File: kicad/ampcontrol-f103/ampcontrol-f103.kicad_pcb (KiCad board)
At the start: 2 copper layers, 89.3 x 55 mm, 69 parts, among them J1 SP, J10 Buttons, J11 Encoder, J12 LCD_CTRL, J13 I2C, J14 I2C, J15 I2C, J16 SPI_2.4, J17 SPI_2.8, J18 SPI_3.2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

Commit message: Kicad PCB: Fix missing connection for sdcard socket
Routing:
- net /SD_SCK: track 109.1 -> 115.7 mm
- net /SD_MOSI: track 124.4 -> 127.7 mm
- net /SD_MISO: track 118.9 -> 122.2 mm
- net /SD_CS: track 126.0 -> 129.3 mm
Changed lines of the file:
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@@
     (thickness 1.6)
     (drawings 35)
-    (tracks 1268)
+    (tracks 1273)
     (zones 0)
     (modules 69)
@@
   )
   (setup
-    (last_trace_width 0.25)
+    (last_trace_width 0.6)
     (user_trace_width 0.4)
     (user_trace_width 0.6)
@@
   (segment (start 172.239988 102.809988) (end 143.203012 102.809988) (width 0.4) (layer F.Cu) (net 30))
   (segment (start 169.92 77.32) (end 171.85 77.32) (width 0.4) (layer F.Cu) (net 30))
+  (segment (start 177.74 77.32) (end 181.04 77.32) (width 0.6) (layer F.Cu) (net 30))
   (segment (start 125.17 64.31) (end 122.63 66.85) (width 0.4) (layer B.Cu) (net 31) (status 20))
   (segment (start 125.17 63.04) (end 125.17 64.31) (width 0.4) (layer B.Cu) (net 31) (status 10))
@@
   (segment (start 173.340011 84.259989) (end 173.340011 102.558531) (width 0.4) (layer F.Cu) (net 56))
   (segment (start 177.74 79.86) (end 173.340011 84.259989) (width 0.4) (layer F.Cu) (net 56))
+  (segment (start 177.74 79.86) (end 181.04 79.86) (width 0.6) (layer F.Cu) (net 56))
   (segment (start 129.595 77.105) (end 129.595 75.4388) (width 0.25) (layer F.Cu) (net 57) (status 10))
   (segment (start 129.595 74.636741) (end 132.15173 72.080011) (width 0.25) (layer F.Cu) (net 57))
@@
   (segment (start 174.339988 102.461469) (end 172.752458 104.048999) (width 0.4) (layer F.Cu) (net 57))
   (segment (start 177.74 82.4) (end 176.537919 82.4) (width 0.4) (layer F.Cu) (net 57))
+  (segment (start 177.74 82.4) (end 181.04 82.4) (width 0.6) (layer F.Cu) (net 57))
   (segment (start 130.095 75.9645) (end 130.095 77.105) (width 0.25) (layer F.Cu) (net 58) (status 20))
   (segment (start 130.095 77.105) (end 130.095 75.875) (width 0.25) (layer F.Cu) (net 58) (status 10))
@@
   (segment (start 175.71 84.94) (end 174.939999 85.710001) (width 0.4) (layer F.Cu) (net 58))
   (segment (start 177.74 84.94) (end 175.71 84.94) (width 0.4) (layer F.Cu) (net 58))
+  (segment (start 177.74 84.94) (end 181.04 84.94) (width 0.6) (layer F.Cu) (net 58))
+  (segment (start 177.74 84.94) (end 181.04 84.94) (width 0.6) (layer B.Cu) (net 58))
   (segment (start 168.65 90.02) (end 166.4125 90.02) (width 0.25) (layer B.Cu) (net 59) (status 30))
   (segment (start 168.65 92.56) (end 166.4125 92.56) (width 0.25) (layer B.Cu) (net 60) (status 30))

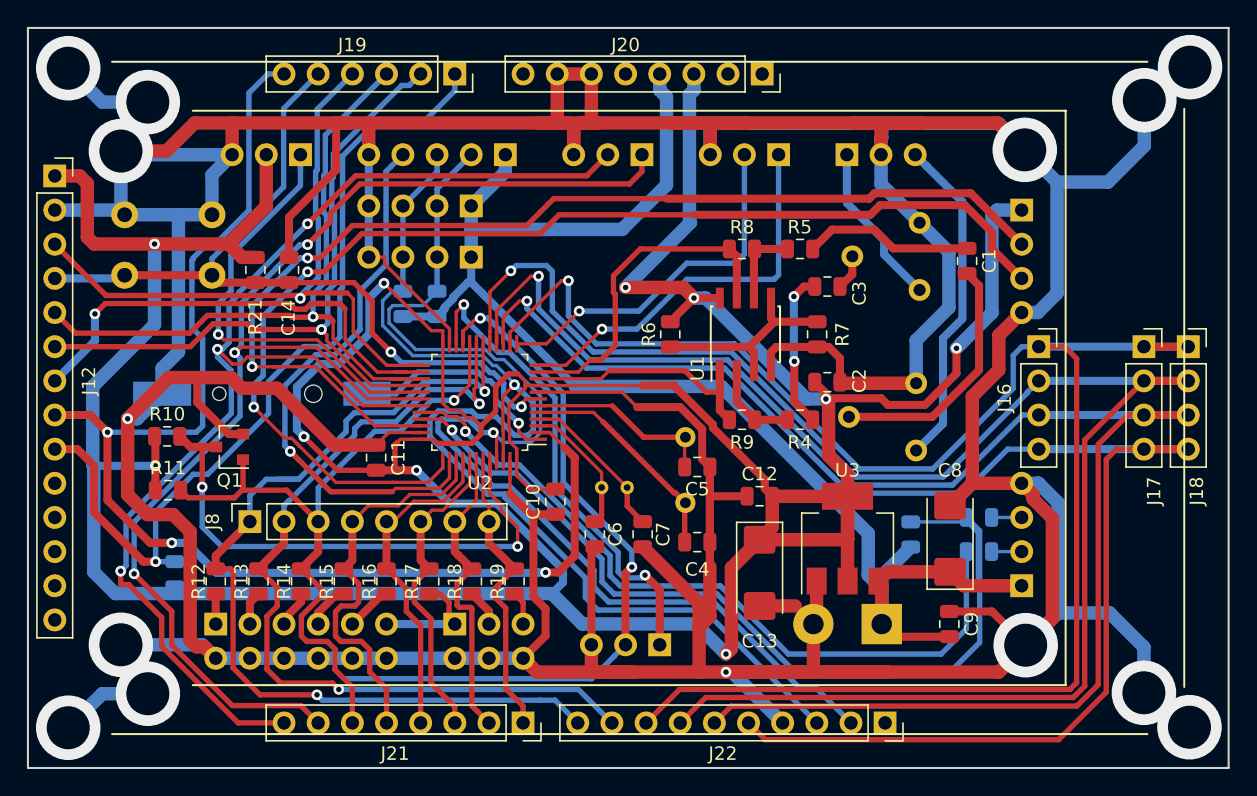
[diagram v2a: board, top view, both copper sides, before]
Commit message: Kicad: Fix arduino-specific pinout
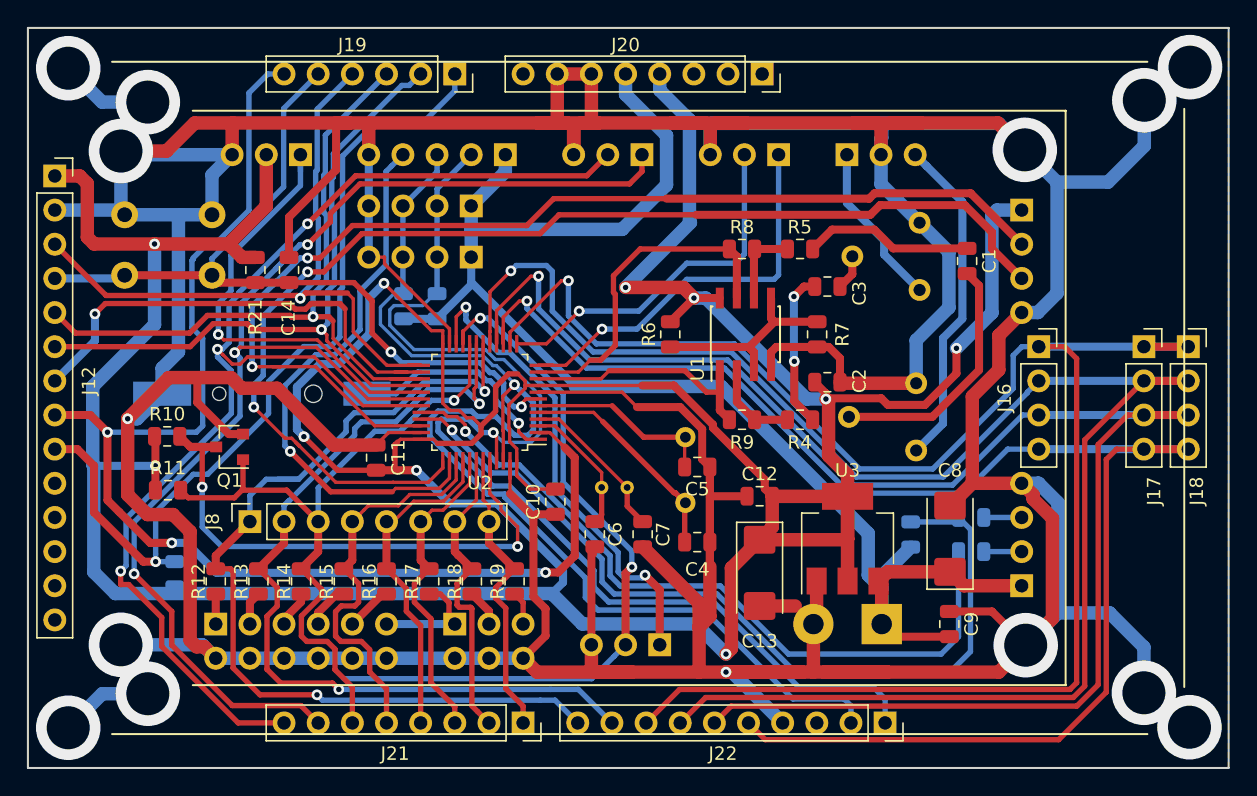
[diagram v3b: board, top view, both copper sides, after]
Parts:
- moved R1 0.58 mm to (164.9, 92.6)
- moved R2 0.58 mm to (164.9, 90.0)
- moved R22 0.18 mm to (122.7, 74.3)
- moved R23 0.17 mm to (125.2, 74.3)
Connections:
- J20 pad 3: +3V3 -> Net-(J20-Pad3)
- J20 pad 4: +5V -> +3V3
- J20 pad 5: Net-(J20-Pad5) -> +5V
- J22 pad 1: Net-(J22-Pad1) -> /SCL
- J22 pad 2: /SCL -> /SDA
- J22 pad 3: /SDA -> Net-(J22-Pad3)
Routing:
- net /USB_DP: track 70.4 -> 64.3 mm
- net /SCL: track 84.6 -> 88.4 mm
- net /SDA: track 85.3 -> 88.6 mm
- net +5V: track 116.5 -> 117.6 mm
- net +3V3: track 345.1 -> 345.8 mm
- net /USB_P: track 2.24 -> 2.82 mm
- net /USB_M: track 2.24 -> 2.82 mm

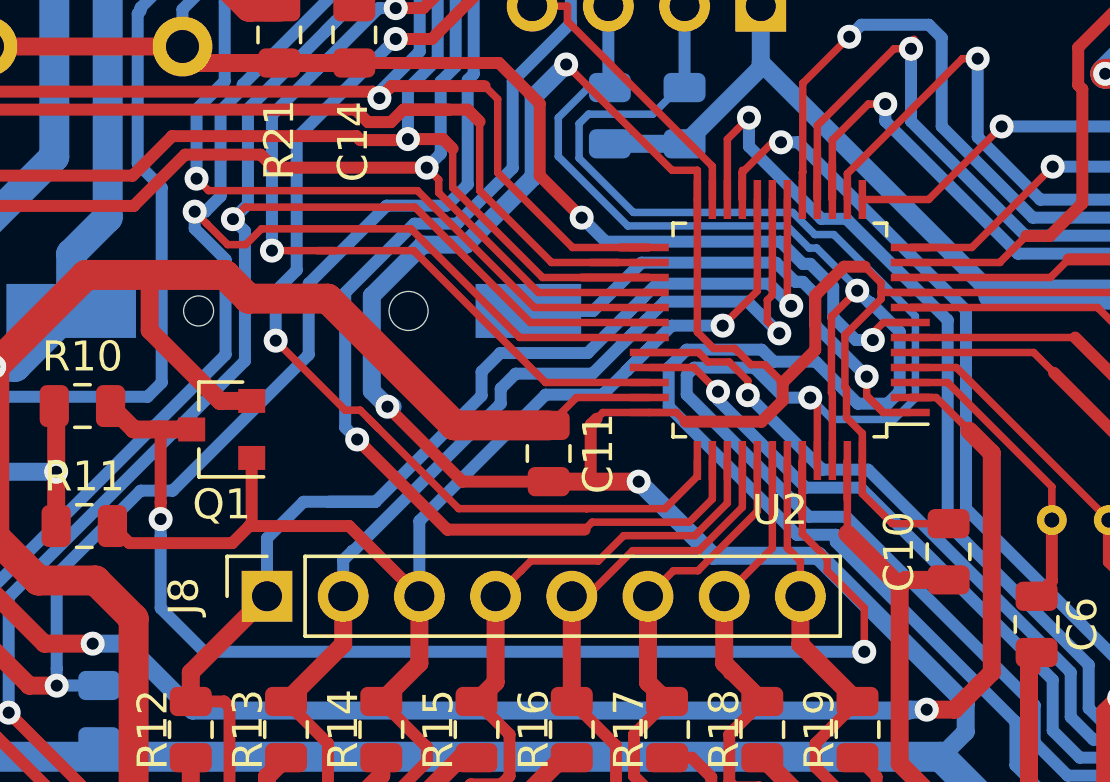
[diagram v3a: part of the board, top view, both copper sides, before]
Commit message: Smal fix for CR1220 package
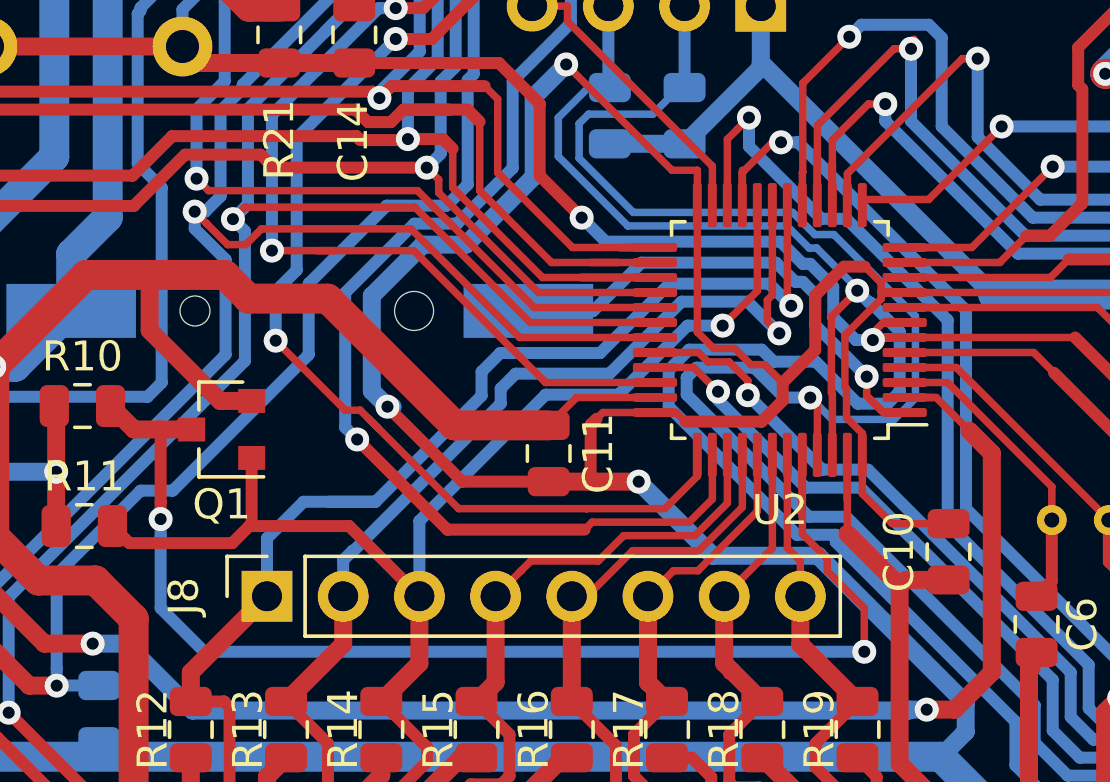
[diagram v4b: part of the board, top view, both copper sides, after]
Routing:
- net /DB1: track 65.8 -> 64.7 mm
- net /DB2: track 54.7 -> 53.6 mm
- net /DB0: track 71.2 -> 70.4 mm

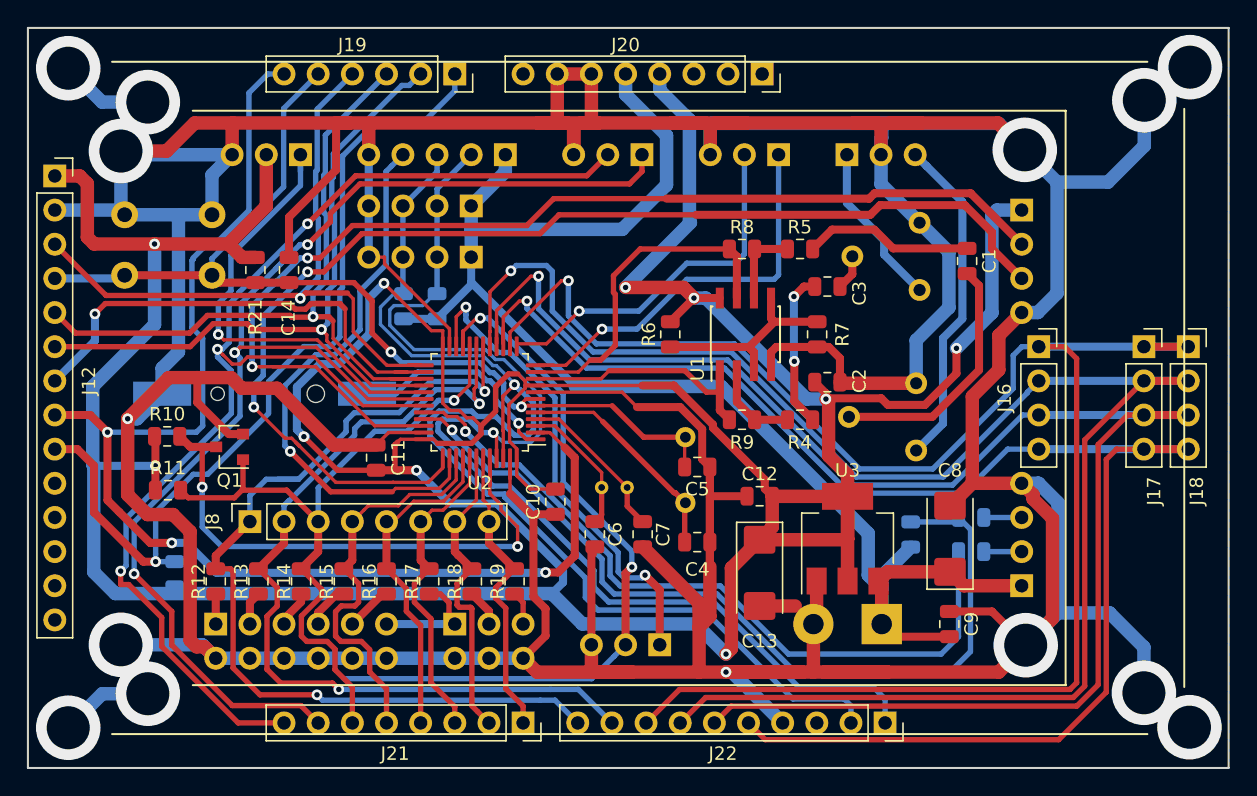
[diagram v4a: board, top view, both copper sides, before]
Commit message: Fix PCB bugs
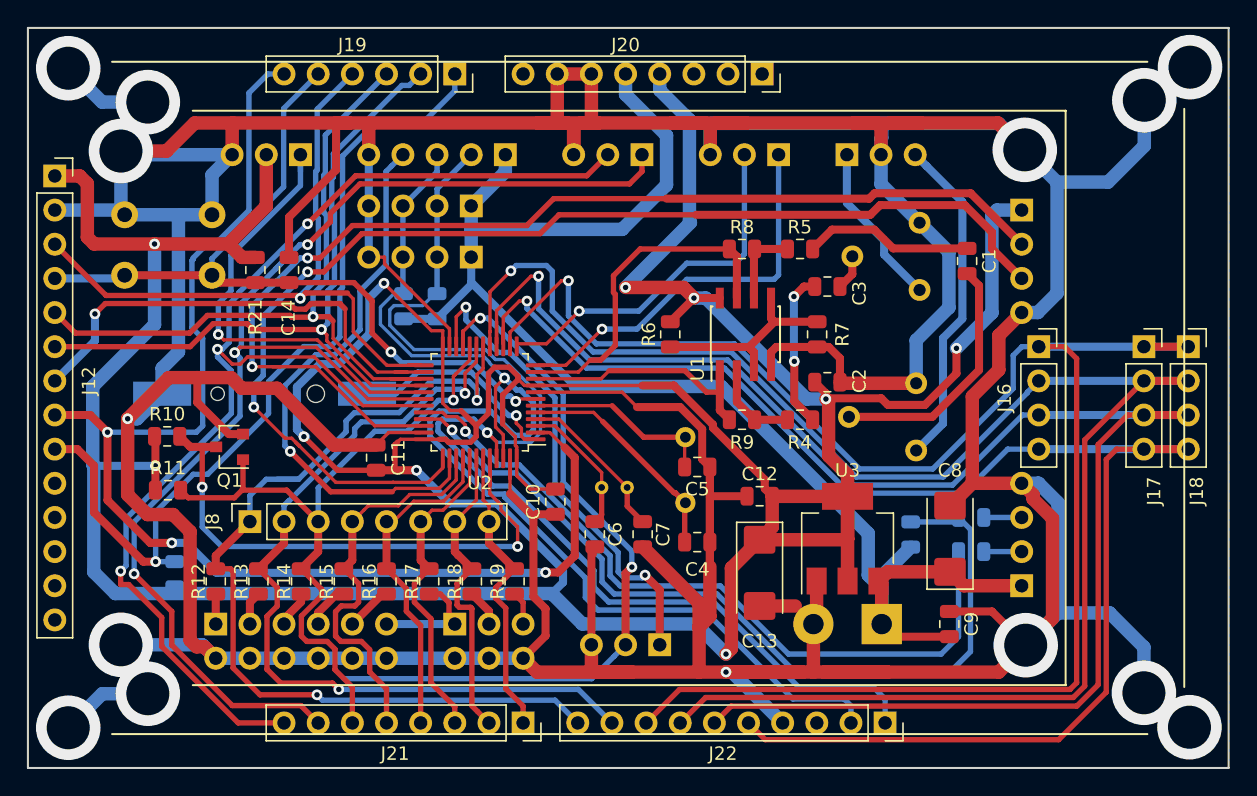
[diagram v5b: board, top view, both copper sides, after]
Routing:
- net /DB1: track 64.7 -> 62.7 mm
- net +3V3: track 345.8 -> 347.3 mm
- net /NRST: track 60.7 -> 59.5 mm
- net /DB0: track 70.4 -> 71.4 mm
- net /SCL: track 88.4 -> 89.2 mm

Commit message: Schematic: map MUTE/STBY to PB11/PB10, that are de-facto have been used
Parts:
- J2: value MUTE_STBY -> SWD
- J6: value UART3 -> STBY_MUTE
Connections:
- J2 pad 2: /MUTE -> /SWDIO
- J2 pad 3: /STBY -> /SWCLK
- J6 pad 1: /TX3 -> /STBY
- J6 pad 2: /RX3 -> /MUTE
- U2 pad 21: /RX3 -> /MUTE
- U2 pad 22: /TX3 -> /STBY
- U2 pad 34: /MUTE -> /SWDIO
- U2 pad 37: /STBY -> /SWCLK
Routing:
- net /SWCLK: track 0.00 -> 87.6 mm, vias 0 -> 2
- net /SWDIO: track 0.00 -> 82.3 mm, vias 0 -> 2
- net /RX3: track 55.5 -> 0.00 mm, vias 2 -> 0
- net /STBY: track 87.6 -> 35.8 mm
- net /TX3: track 35.8 -> 0.00 mm, vias 2 -> 0
- net /MUTE: track 82.3 -> 55.5 mm

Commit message: Small changes in schematic/PCB
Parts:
- added R24: 0, Resistor_SMD:R_0805_2012Metric, F.Cu at (102.4, 74.8)
- added R25: 0, Resistor_SMD:R_0805_2012Metric, F.Cu at (102.4, 77.4)
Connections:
- J12 pad 4: /NRST -> /RST
- J19 pad 5: /NRST -> /RST
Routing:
- net /RST: track 0.00 -> 36.7 mm, vias 0 -> 2
- net /NRST: track 59.5 -> 39.1 mm
- net /HW_RST: track 41.5 -> 59.6 mm, vias 1 -> 2
- net GNDD: track 622.8 -> 615.3 mm
- net /RS: track 55.4 -> 62.2 mm
- net /WR: track 52.7 -> 58.0 mm
- net /SCK: track 37.0 -> 32.6 mm
- net +3V3: track 347.3 -> 350.4 mm
- net /CS: track 53.2 -> 55.3 mm
- net /RX1: track 93.1 -> 91.3 mm
- net /TX1: track 95.1 -> 94.2 mm
- net /BCKL: track 96.2 -> 95.5 mm
- net /RD: track 63.8 -> 64.4 mm
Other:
- board text added: "+ -"

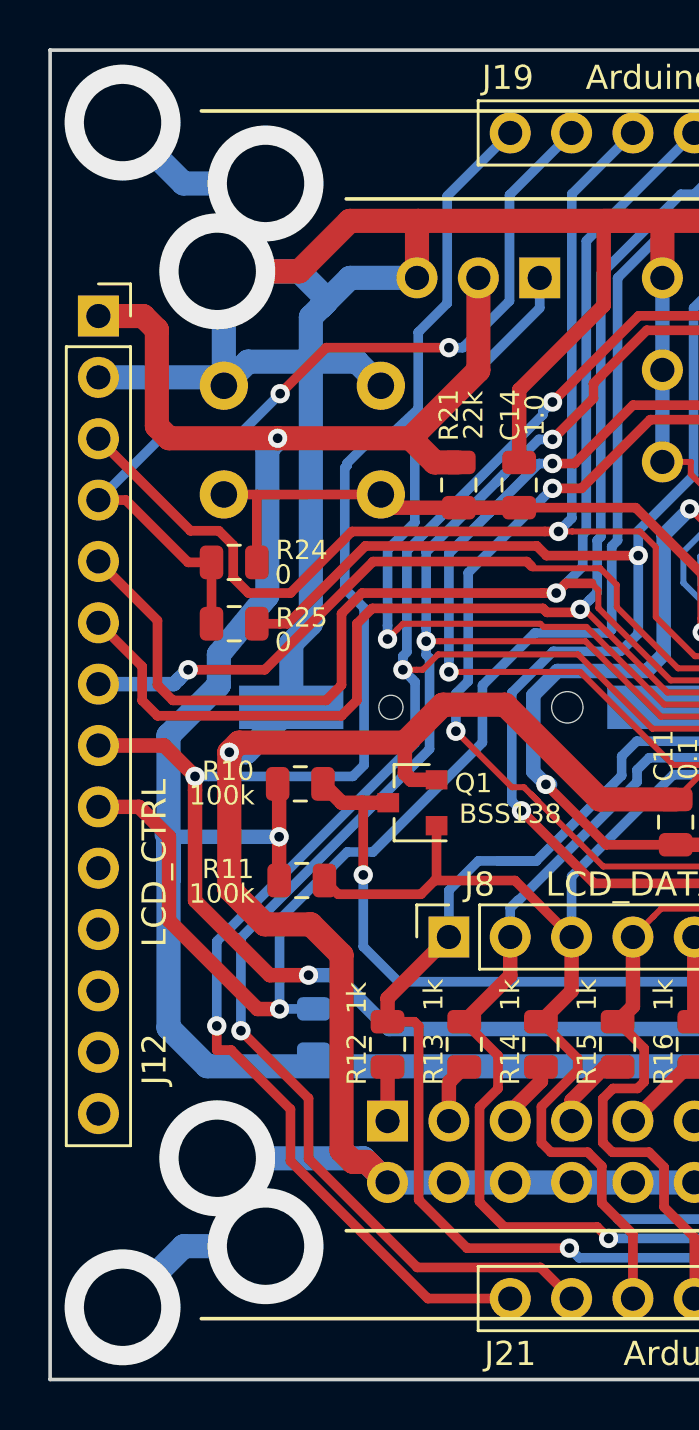
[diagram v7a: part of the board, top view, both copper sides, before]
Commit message: Fix mounting holes on PCB for 2.8 display
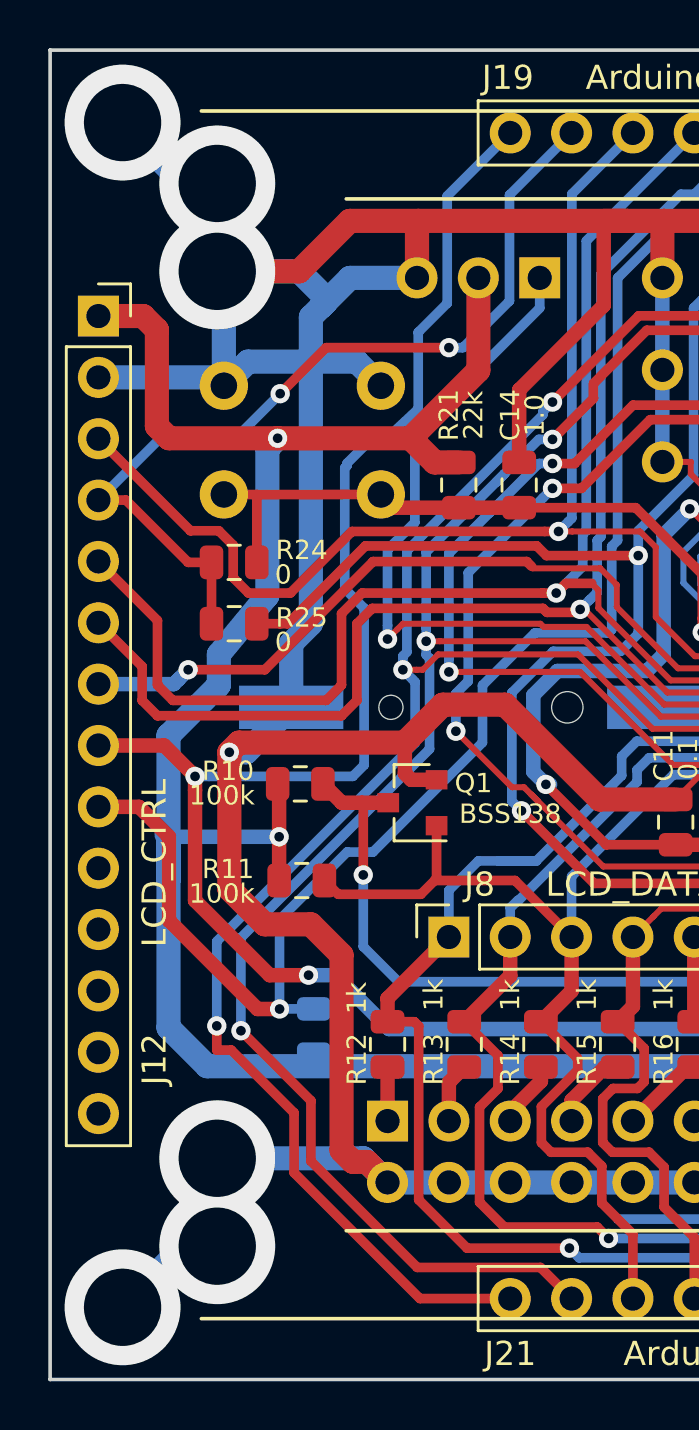
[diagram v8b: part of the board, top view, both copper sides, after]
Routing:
- net GNDD: track 615.3 -> 608.9 mm
